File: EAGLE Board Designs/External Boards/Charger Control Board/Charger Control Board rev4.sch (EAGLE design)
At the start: 83 parts

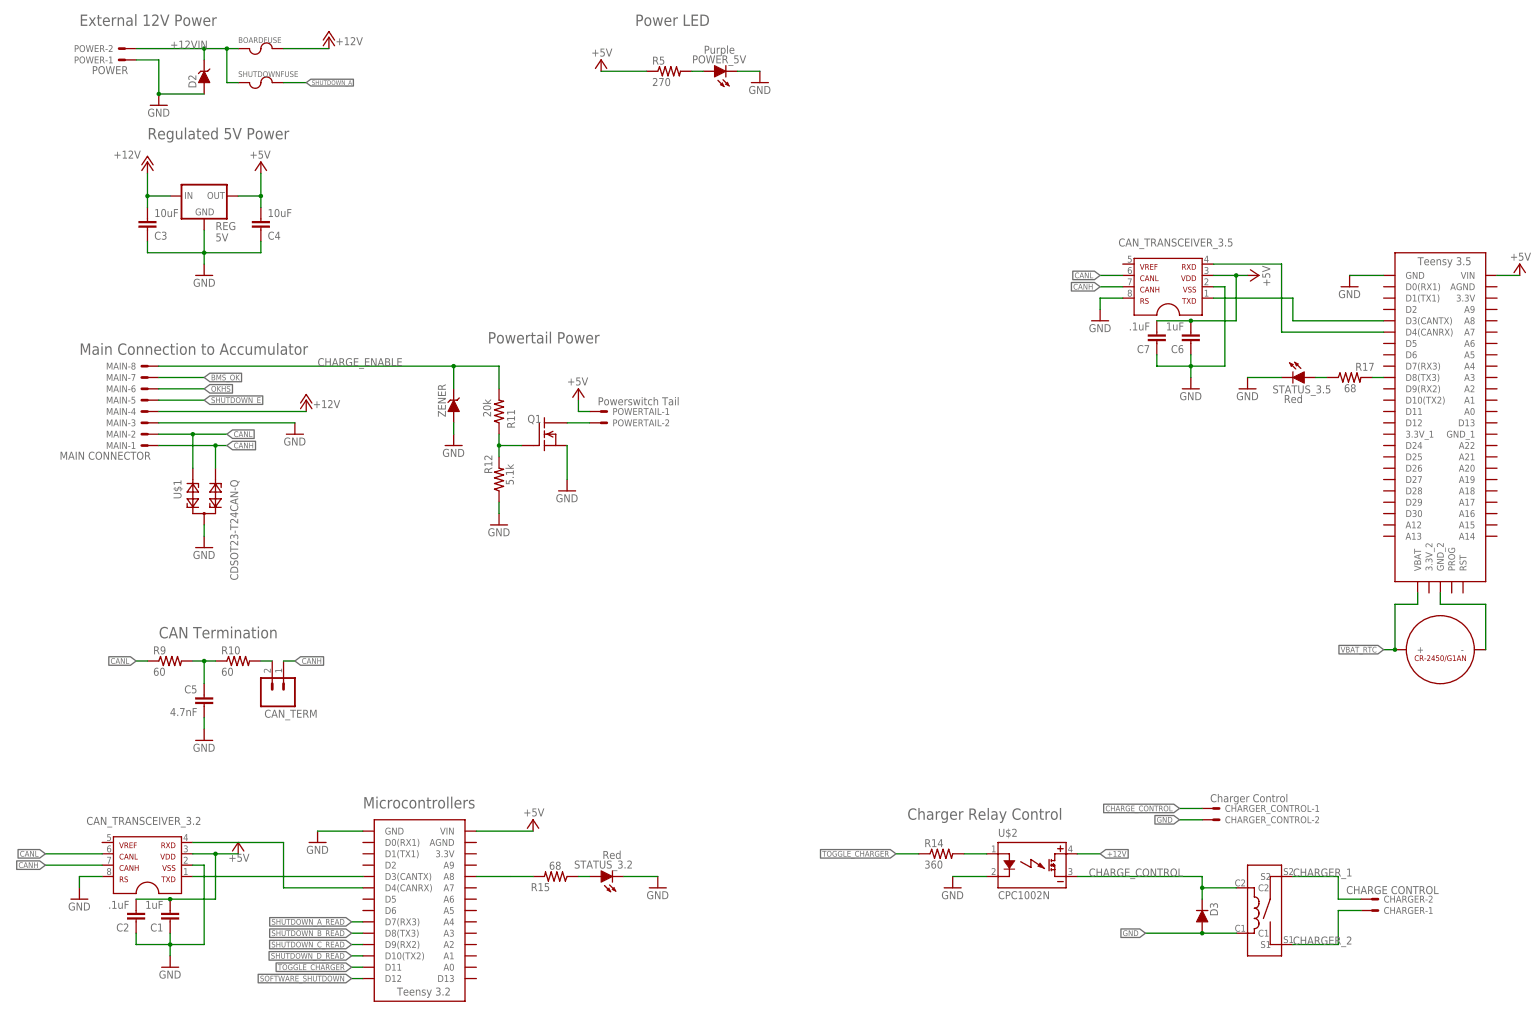
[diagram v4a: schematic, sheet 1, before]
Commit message: Updated locations of componenets and teensy symbol
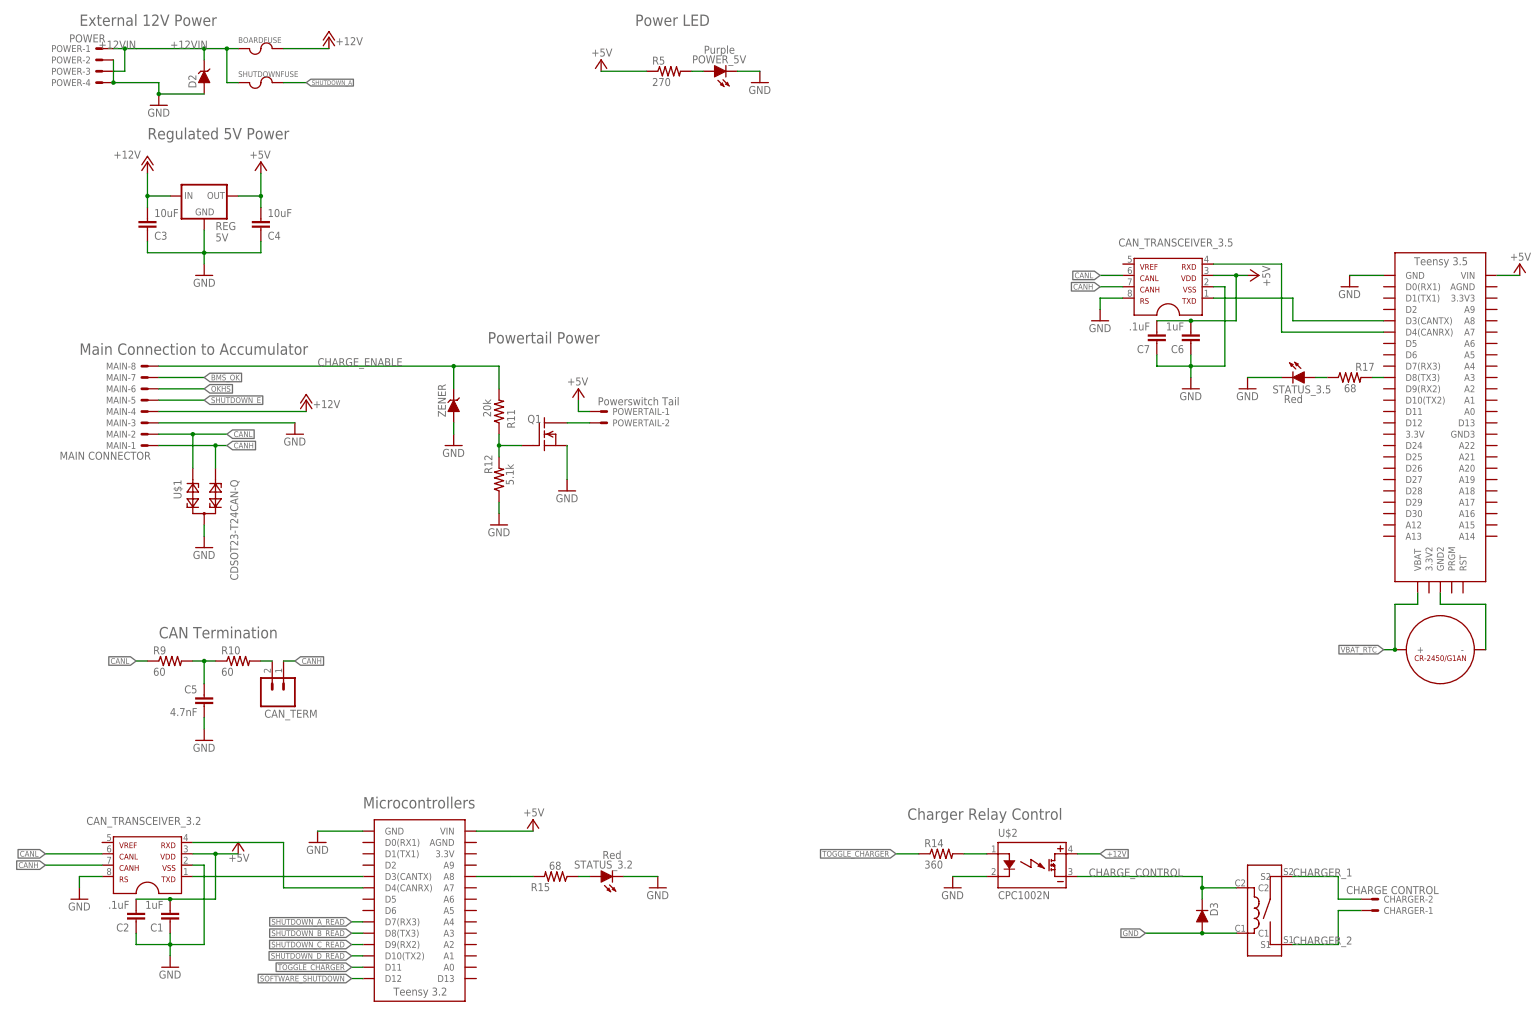
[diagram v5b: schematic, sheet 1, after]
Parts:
- removed CHARGER_CONTROL: Charger Control, HyTechDevices:CONNECTOR-2NANO-FIT_VERTICAL-2
- added X1: LATCHING, HyTechDevices:CONNECTOR-2NANO-FIT_VERTICAL-2
- POWER: device HyTechDevices:CONNECTOR-2NANO-FIT_VERTICAL-2 -> HyTechDevices:CONNECTOR-4NANO-FIT-VERTICAL-4
- U$5: value TEENSY_3.5_EXT -> TEENSY_3.5_EXT_RTC; device HyTechDevices:TEENSY_3.5_EXT -> HyTechDevices:TEENSY_3.5_EXT_RTC
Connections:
- net +12VIN: now also POWER-1.S, POWER-3.S; no longer POWER-2.S
- net CHARGE_CONTROL: no longer CHARGER_CONTROL-1.S
- net GND: now also POWER-2.S, POWER-4.S, X1-1.S; no longer CHARGER_CONTROL-2.S, POWER-1.S
- net LATCH_EXT_BUTTON: now also X1-2.S
- net N$61: now also U$5.GND2; no longer U$5.GND_2
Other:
- moved on the sheet: POWER-1, POWER-2
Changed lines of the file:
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@@
 <part name="U$3" library="HyTechDevices" deviceset="KT12-1A-40L-THT" device=""/>
 <part name="CHARGER" library="HyTechDevices" deviceset="CONNECTOR-2" device="NANO-FIT_VERTICAL-2" value="CHARGE CONTROL"/>
-<part name="U$5" library="HyTechDevices" deviceset="TEENSY_3.5_EXT" device=""/>
+<part name="U$5" library="HyTechDevices" deviceset="TEENSY_3.5_EXT_RTC" device=""/>
 <part name="CAN_TRANSCEIVER_3.5" library="HyTechDevices" deviceset="MCP2551" device="" value="MCP2551"/>
 <part name="GND11" library="HyTechSymbols" deviceset="GND" device=""/>
@@
 </part>
 <part name="P+5" library="supply1" deviceset="+12V" device=""/>
-<part name="POWER" library="HyTechDevices" deviceset="CONNECTOR-2" device="NANO-FIT_VERTICAL-2" value="POWER"/>
 <part name="GND2" library="supply1" deviceset="GND" device=""/>
 <part name="REG" library="HyTechDevices" deviceset="OKI-78SR-5" device="" value="5V"/>
@@
 <part name="GND25" library="HyTechSymbols" deviceset="GND" device=""/>
 <part name="D2" library="HyTechDevices" deviceset="DIODE_ZENER" device="0603"/>
-<part name="CHARGER_CONTROL" library="HyTechDevices" deviceset="CONNECTOR-2" device="NANO-FIT_VERTICAL-2" value="Charger Control"/>
+<part name="POWER" library="HyTechDevices" deviceset="CONNECTOR-4" device="NANO-FIT-VERTICAL-4" value="POWER"/>
+<part name="X1" library="HyTechDevices" deviceset="CONNECTOR-2" device="NANO-FIT_VERTICAL-2" value="LATCHING"/>
+<part name="GND28" library="HyTechSymbols" deviceset="GND" device=""/>
 </parts>
 <sheets>
@@
 <attribute name="VALUE" x="96.52" y="251.46" size="1.778" layer="96" rot="R180"/>
 </instance>
-<instance part="POWER" gate="-2" x="43.18" y="248.92" smashed="yes" rot="R180">
-<attribute name="NAME" x="40.64" y="249.682" size="1.524" layer="95" rot="R180"/>
-</instance>
-<instance part="POWER" gate="-1" x="43.18" y="246.38" smashed="yes" rot="R180">
-<attribute name="NAME" x="40.64" y="247.142" size="1.524" layer="95" rot="R180"/>
-<attribute name="VALUE" x="43.942" y="244.983" size="1.778" layer="96" rot="R180"/>
-</instance>
 <instance part="GND2" gate="1" x="50.8" y="236.22" smashed="yes">
 <attribute name="VALUE" x="48.26" y="233.68" size="1.778" layer="96"/>
@@
 <attribute name="NAME" x="59.2074" y="240.03" size="1.778" layer="95" rot="R90"/>
 </instance>
-<instance part="CHARGER_CONTROL" gate="-2" x="287.02" y="76.2" smashed="yes">
-<attribute name="NAME" x="289.56" y="75.438" size="1.524" layer="95"/>
-</instance>
-<instance part="CHARGER_CONTROL" gate="-1" x="287.02" y="78.74" smashed="yes">
-<attribute name="NAME" x="289.56" y="77.978" size="1.524" layer="95"/>
-<attribute name="VALUE" x="286.258" y="80.137" size="1.778" layer="96"/>
+<instance part="POWER" gate="-1" x="38.1" y="248.92" smashed="yes" rot="MR0">
+<attribute name="NAME" x="35.56" y="248.158" size="1.524" layer="95" rot="MR0"/>
+<attribute name="VALUE" x="38.862" y="250.317" size="1.778" layer="96" rot="MR0"/>
+</instance>
+<instance part="POWER" gate="-2" x="38.1" y="246.38" smashed="yes" rot="MR0">
+<attribute name="NAME" x="35.56" y="245.618" size="1.524" layer="95" rot="MR0"/>
+</instance>
+<instance part="POWER" gate="-3" x="38.1" y="243.84" smashed="yes" rot="MR0">
+<attribute name="NAME" x="35.56" y="243.078" size="1.524" layer="95" rot="MR0"/>
+</instance>
+<instance part="POWER" gate="-4" x="38.1" y="241.3" smashed="yes" rot="MR0">
+<attribute name="NAME" x="35.56" y="240.538" size="1.524" layer="95" rot="MR0"/>
 </instance>
 </instances>
@@
 <segment>
 <pinref part="GND2" gate="1" pin="GND"/>
-<wire x1="50.8" y1="238.76" x2="50.8" y2="246.38" width="0.1524" layer="91"/>
-<wire x1="50.8" y1="246.38" x2="45.72" y2="246.38" width="0.1524" layer="91"/>
-<pinref part="POWER" gate="-1" pin="S"/>
+<wire x1="50.8" y1="238.76" x2="50.8" y2="241.3" width="0.1524" layer="91"/>
 <pinref part="D2" gate="G$1" pin="A"/>
 <wire x1="50.8" y1="238.76" x2="60.96" y2="238.76" width="0.1524" layer="91"/>
 <junction x="50.8" y="238.76"/>
+<pinref part="POWER" gate="-2" pin="S"/>
+<pinref part="POWER" gate="-4" pin="S"/>
+<wire x1="40.64" y1="246.38" x2="40.64" y2="241.3" width="0.1524" layer="91"/>
+<junction x="40.64" y="241.3"/>
+<wire x1="40.64" y1="241.3" x2="50.8" y2="241.3" width="0.1524" layer="91"/>
 </segment>
 <segment>
@@
 <wire x1="48.26" y1="203.2" x2="60.96" y2="203.2" width="0.1524" layer="91"/>
 </segment>
-<segment>
-<pinref part="CHARGER_CONTROL" gate="-2" pin="S"/>
-<wire x1="284.48" y1="76.2" x2="279.4" y2="76.2" width="0.1524" layer="91"/>
-<label x="279.4" y="76.2" size="1.27" layer="95" font="vector" rot="R180" xref="yes"/>
-</segment>
 </net>
 <net name="CANH" class="0">
@@
 <wire x1="292.1" y1="60.96" x2="284.48" y2="60.96" width="0.1524" layer="91"/>
 <junction x="284.48" y="60.96"/>
-</segment>
-<segment>
-<pinref part="CHARGER_CONTROL" gate="-1" pin="S"/>
-<wire x1="284.48" y1="78.74" x2="279.4" y2="78.74" width="0.1524" layer="91"/>
-<label x="279.4" y="78.74" size="1.27" layer="95" font="vector" rot="R180" xref="yes"/>
 </segment>
 </net>
@@
 <pinref part="U$16" gate="G$1" pin="-"/>
 <wire x1="347.98" y1="124.46" x2="347.98" y2="114.3" width="0.1524" layer="91"/>
-<pinref part="U$5" gate="G$1" pin="GND_2"/>
+<pinref part="U$5" gate="G$1" pin="GND2"/>
 </segment>
 </net>
@@
 <wire x1="68.58" y1="241.3" x2="66.04" y2="241.3" width="0.1524" layer="91"/>
 <wire x1="66.04" y1="241.3" x2="66.04" y2="248.92" width="0.1524" layer="91"/>
-<pinref part="POWER" gate="-2" pin="S"/>
 <wire x1="66.04" y1="248.92" x2="60.96" y2="248.92" width="0.1524" layer="91"/>
 <label x="53.34" y="248.92" size="1.778" layer="95"/>
@@
 <wire x1="60.96" y1="246.38" x2="60.96" y2="248.92" width="0.1524" layer="91"/>
 <junction x="60.96" y="248.92"/>
+<pinref part="POWER" gate="-3" pin="S"/>
+<wire x1="40.64" y1="243.84" x2="43.18" y2="243.84" width="0.1524" layer="91"/>
+<pinref part="POWER" gate="-1" pin="S"/>
+<wire x1="40.64" y1="248.92" x2="43.18" y2="248.92" width="0.1524" layer="91"/>
+<wire x1="43.18" y1="243.84" x2="43.18" y2="248.92" width="0.1524" layer="91"/>
+<wire x1="43.18" y1="248.92" x2="45.72" y2="248.92" width="0.1524" layer="91"/>
+<junction x="43.18" y="248.92"/>
+<label x="45.72" y="248.92" size="1.778" layer="95" rot="MR0"/>
 </segment>
 </net>
@@
 <attribute name="VALUE" x="127" y="121.92" size="1.778" layer="96"/>
 </instance>
+<instance part="X1" gate="-2" x="106.68" y="208.28" smashed="yes" rot="R180">
+<attribute name="NAME" x="104.14" y="209.042" size="1.524" layer="95" rot="R180"/>
+</instance>
+<instance part="X1" gate="-1" x="106.68" y="205.74" smashed="yes" rot="R180">
+<attribute name="NAME" x="104.14" y="206.502" size="1.524" layer="95" rot="R180"/>
+<attribute name="VALUE" x="107.442" y="204.343" size="1.778" layer="96" rot="R180"/>
+</instance>
+<instance part="GND28" gate="1" x="111.76" y="200.66" smashed="yes">
+<attribute name="VALUE" x="109.22" y="198.12" size="1.778" layer="96"/>
+</instance>
 </instances>
 <busses>
@@
 <wire x1="129.54" y1="129.54" x2="129.54" y2="127" width="0.1524" layer="91"/>
 <pinref part="R31" gate="G$1" pin="2"/>
+</segment>
+<segment>
+<pinref part="X1" gate="-1" pin="S"/>
+<wire x1="109.22" y1="205.74" x2="111.76" y2="205.74" width="0.1524" layer="91"/>
+<wire x1="111.76" y1="205.74" x2="111.76" y2="203.2" width="0.1524" layer="91"/>
+<pinref part="GND28" gate="1" pin="GND"/>
 </segment>
 </net>
@@
 <label x="86.36" y="210.82" size="1.778" layer="95"/>
 <pinref part="D9" gate="1" pin="C"/>
-<wire x1="104.14" y1="210.82" x2="114.3" y2="210.82" width="0.1524" layer="91"/>
+<wire x1="104.14" y1="210.82" x2="109.22" y2="210.82" width="0.1524" layer="91"/>
+<wire x1="109.22" y1="210.82" x2="114.3" y2="210.82" width="0.1524" layer="91"/>
 <wire x1="104.14" y1="210.82" x2="104.14" y2="241.3" width="0.1524" layer="91"/>
 <wire x1="104.14" y1="241.3" x2="149.86" y2="241.3" width="0.1524" layer="91"/>
 <junction x="104.14" y="210.82"/>
 <label x="116.84" y="241.3" size="1.778" layer="95"/>
-</segment>
-</net>
+<pinref part="X1" gate="-2" pin="S"/>
+<wire x1="109.22" y1="210.82" x2="109.22" y2="208.28" width="0.1524" layer="91"/>
+<junction x="109.22" y="210.82"/>
+</segment>
+</net>

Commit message: Finished top placement
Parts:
- renumbered CHARGER to CHARGE, S1 to LATCH_BUTTON, X1 to LATCHING
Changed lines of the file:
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@@
 <part name="OKHS" library="HyTechDevices" deviceset="LED" device="-0805" value="Yellow"/>
 <part name="GND24" library="HyTechSymbols" deviceset="GND" device=""/>
-<part name="S1" library="HyTechDevices" deviceset="BTN_10-XX" device="SMD"/>
+<part name="LATCH_BUTTON" library="HyTechDevices" deviceset="BTN_10-XX" device="SMD"/>
 <part name="GND5" library="HyTechSymbols" deviceset="GND" device=""/>
 <part name="R6" library="HyTechDevices" deviceset="RESISTOR" device="0603-RES" value="5.1k">
@@
 <part name="D3" library="HyTechDevices" deviceset="DIODE" device="0805" value="DIODE"/>
 <part name="U$3" library="HyTechDevices" deviceset="KT12-1A-40L-THT" device=""/>
-<part name="CHARGER" library="HyTechDevices" deviceset="CONNECTOR-2" device="NANO-FIT_VERTICAL-2" value="CHARGE CONTROL"/>
+<part name="CHARGE" library="HyTechDevices" deviceset="CONNECTOR-2" device="NANO-FIT_VERTICAL-2" value="CHARGE CONTROL"/>
 <part name="U$5" library="HyTechDevices" deviceset="TEENSY_3.5_EXT_RTC" device=""/>
 <part name="CAN_TRANSCEIVER_3.5" library="HyTechDevices" deviceset="MCP2551" device="" value="MCP2551"/>
@@
 <part name="D2" library="HyTechDevices" deviceset="DIODE_ZENER" device="0603"/>
 <part name="POWER" library="HyTechDevices" deviceset="CONNECTOR-4" device="NANO-FIT-VERTICAL-4" value="POWER"/>
-<part name="X1" library="HyTechDevices" deviceset="CONNECTOR-2" device="NANO-FIT_VERTICAL-2" value="LATCHING"/>
+<part name="LATCHING" library="HyTechDevices" deviceset="CONNECTOR-2" device="NANO-FIT_VERTICAL-2" value="LATCHING"/>
 <part name="GND28" library="HyTechSymbols" deviceset="GND" device=""/>
 </parts>
@@
 </instance>
 <instance part="U$3" gate="G$1" x="302.26" y="45.72" smashed="yes" rot="R90"/>
-<instance part="CHARGER" gate="-2" x="322.58" y="58.42" smashed="yes" rot="MR180">
+<instance part="CHARGE" gate="-2" x="322.58" y="58.42" smashed="yes" rot="MR180">
 <attribute name="NAME" x="325.12" y="59.182" size="1.524" layer="95" rot="MR180"/>
 </instance>
-<instance part="CHARGER" gate="-1" x="322.58" y="55.88" smashed="yes" rot="MR180">
+<instance part="CHARGE" gate="-1" x="322.58" y="55.88" smashed="yes" rot="MR180">
 <attribute name="NAME" x="325.12" y="56.642" size="1.524" layer="95" rot="MR180"/>
 <attribute name="VALUE" x="316.738" y="59.563" size="1.778" layer="96" rot="MR180" align="top-left"/>
@@
 <pinref part="U$3" gate="G$1" pin="S2"/>
 <wire x1="304.8" y1="63.5" x2="314.96" y2="63.5" width="0.1524" layer="91"/>
-<pinref part="CHARGER" gate="-2" pin="S"/>
+<pinref part="CHARGE" gate="-2" pin="S"/>
 <wire x1="320.04" y1="58.42" x2="314.96" y2="58.42" width="0.1524" layer="91"/>
 <wire x1="314.96" y1="63.5" x2="314.96" y2="58.42" width="0.1524" layer="91"/>
@@
 <net name="CHARGER_1" class="0">
 <segment>
-<pinref part="CHARGER" gate="-1" pin="S"/>
+<pinref part="CHARGE" gate="-1" pin="S"/>
 <wire x1="320.04" y1="55.88" x2="314.96" y2="55.88" width="0.1524" layer="91"/>
 <pinref part="U$3" gate="G$1" pin="S1"/>
@@
 <attribute name="VALUE" x="83.312" y="216.535" size="1.778" layer="96" rot="R180"/>
 </instance>
-<instance part="S1" gate="1" x="119.38" y="210.82" smashed="yes" rot="R270">
+<instance part="LATCH_BUTTON" gate="1" x="119.38" y="210.82" smashed="yes" rot="R270">
 <attribute name="NAME" x="116.84" y="207.01" size="1.778" layer="95"/>
 <attribute name="VALUE" x="122.555" y="214.63" size="1.778" layer="96"/>
@@
 <attribute name="VALUE" x="127" y="121.92" size="1.778" layer="96"/>
 </instance>
-<instance part="X1" gate="-2" x="106.68" y="208.28" smashed="yes" rot="R180">
+<instance part="LATCHING" gate="-2" x="106.68" y="208.28" smashed="yes" rot="R180">
 <attribute name="NAME" x="104.14" y="209.042" size="1.524" layer="95" rot="R180"/>
 </instance>
-<instance part="X1" gate="-1" x="106.68" y="205.74" smashed="yes" rot="R180">
+<instance part="LATCHING" gate="-1" x="106.68" y="205.74" smashed="yes" rot="R180">
 <attribute name="NAME" x="104.14" y="206.502" size="1.524" layer="95" rot="R180"/>
 <attribute name="VALUE" x="107.442" y="204.343" size="1.778" layer="96" rot="R180"/>
@@
 </segment>
 <segment>
-<pinref part="S1" gate="1" pin="S"/>
-<pinref part="S1" gate="1" pin="S1"/>
+<pinref part="LATCH_BUTTON" gate="1" pin="S"/>
+<pinref part="LATCH_BUTTON" gate="1" pin="S1"/>
 <wire x1="124.46" y1="210.82" x2="124.46" y2="208.28" width="0.1524" layer="91"/>
 <pinref part="GND5" gate="1" pin="GND"/>
@@
 </segment>
 <segment>
-<pinref part="X1" gate="-1" pin="S"/>
+<pinref part="LATCHING" gate="-1" pin="S"/>
 <wire x1="109.22" y1="205.74" x2="111.76" y2="205.74" width="0.1524" layer="91"/>
 <wire x1="111.76" y1="205.74" x2="111.76" y2="203.2" width="0.1524" layer="91"/>
@@
 <segment>
 <pinref part="LATCH" gate="LED" pin="C"/>
-<pinref part="S1" gate="1" pin="P"/>
-<pinref part="S1" gate="1" pin="P1"/>
+<pinref part="LATCH_BUTTON" gate="1" pin="P"/>
+<pinref part="LATCH_BUTTON" gate="1" pin="P1"/>
 <wire x1="114.3" y1="210.82" x2="114.3" y2="208.28" width="0.1524" layer="91"/>
 <junction x="114.3" y="210.82"/>
@@
 <junction x="104.14" y="210.82"/>
 <label x="116.84" y="241.3" size="1.778" layer="95"/>
-<pinref part="X1" gate="-2" pin="S"/>
+<pinref part="LATCHING" gate="-2" pin="S"/>
 <wire x1="109.22" y1="210.82" x2="109.22" y2="208.28" width="0.1524" layer="91"/>
 <junction x="109.22" y="210.82"/>
@@
 </sheet>
 </sheets>
-<errors>
-</errors>
 </schematic>
 </drawing>

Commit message: Adjusted bottom
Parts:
- renumbered U$2 to U1
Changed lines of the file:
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@@
 <part name="GND8" library="HyTechSymbols" deviceset="GND" device=""/>
 <part name="Q1" library="HyTechDevices" deviceset="DMG3406L" device="SOT"/>
-<part name="U$2" library="HyTechDevices" deviceset="CPC1002N" device=""/>
+<part name="U1" library="HyTechDevices" deviceset="CPC1002N" device=""/>
 <part name="GND12" library="HyTechSymbols" deviceset="GND" device=""/>
 <part name="R14" library="HyTechDevices" deviceset="RESISTOR" device="0603-RES" value="360">
@@
 <attribute name="VALUE" x="133.35" y="154.94" size="1.778" layer="95"/>
 </instance>
-<instance part="U$2" gate="G$1" x="246.38" y="66.04" smashed="yes">
+<instance part="U1" gate="G$1" x="246.38" y="66.04" smashed="yes">
 <attribute name="NAME" x="238.76" y="72.39" size="1.778" layer="95" font="vector"/>
 <attribute name="VALUE" x="238.76" y="58.42" size="1.778" layer="96" font="vector"/>
@@
 </segment>
 <segment>
-<pinref part="U$2" gate="G$1" pin="CONTROL-"/>
+<pinref part="U1" gate="G$1" pin="CONTROL-"/>
 <wire x1="236.22" y1="63.5" x2="228.6" y2="63.5" width="0.1524" layer="91"/>
 <pinref part="GND12" gate="1" pin="GND"/>
@@
 <net name="N$10" class="0">
 <segment>
-<pinref part="U$2" gate="G$1" pin="CONTROL+"/>
+<pinref part="U1" gate="G$1" pin="CONTROL+"/>
 <pinref part="R14" gate="G$1" pin="2"/>
 <wire x1="236.22" y1="68.58" x2="231.14" y2="68.58" width="0.1524" layer="91"/>
@@
 <net name="CHARGE_CONTROL" class="0">
 <segment>
-<pinref part="U$2" gate="G$1" pin="DC-"/>
+<pinref part="U1" gate="G$1" pin="DC-"/>
 <wire x1="256.54" y1="63.5" x2="284.48" y2="63.5" width="0.1524" layer="91"/>
 <pinref part="D3" gate="1" pin="C"/>
@@
 <net name="+12V" class="0">
 <segment>
-<pinref part="U$2" gate="G$1" pin="DC+"/>
+<pinref part="U1" gate="G$1" pin="DC+"/>
 <wire x1="256.54" y1="68.58" x2="261.62" y2="68.58" width="0.1524" layer="91"/>
 <label x="261.62" y="68.58" size="1.27" layer="95" xref="yes"/>
